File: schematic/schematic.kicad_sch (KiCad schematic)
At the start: 24 parts, among them SW1 SW_SPST, U1 ESP32-S3-DevKitC

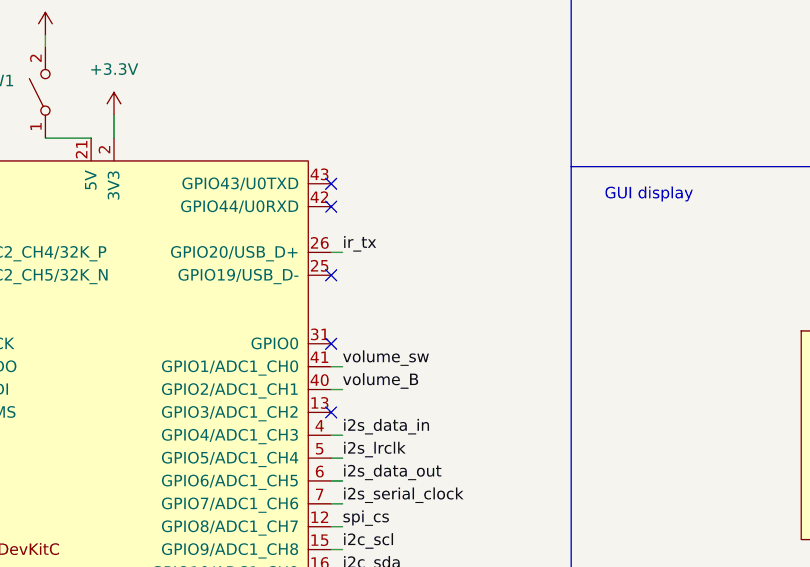
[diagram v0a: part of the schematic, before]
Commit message: Add pullup resistor to gpio 0.  This ensures that strapping pin gpio 0 is high when booting from external 5V supply.  In breadboard testing this did not affect booting from USB jack.
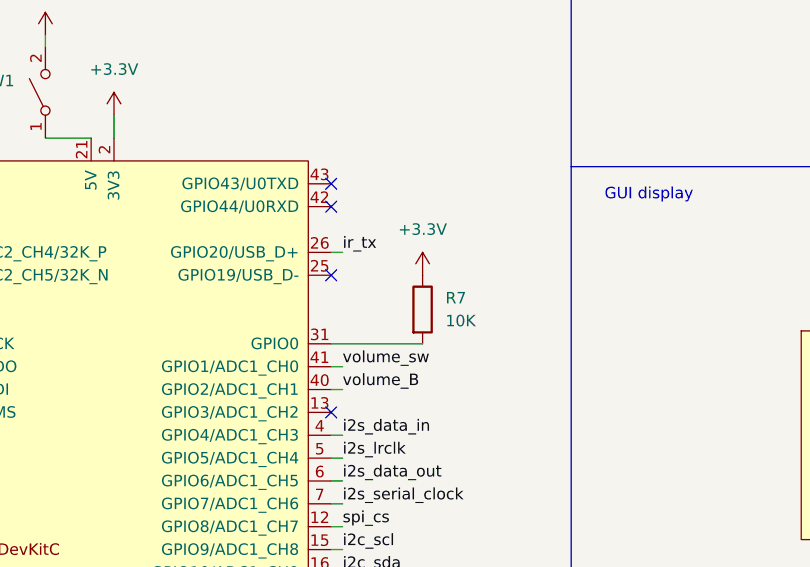
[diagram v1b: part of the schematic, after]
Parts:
- added R7: 10K, symbol Device:R
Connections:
- net +3.3V: now also R7.1
- net at U1.31 (GPIO0): now also R7.2
- no-connect marks 24 -> 23
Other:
- title: Internet Radio V2 -> Internet Radio V3
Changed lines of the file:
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@@
 	(paper "USLetter")
 	(title_block
-		(title "Internet Radio V2")
-		(date "2025-12-01")
-		(rev "2.0")
+		(title "Internet Radio V3")
+		(date "2026-02-24")
+		(rev "3.0")
 		(company "AG Keck")
 	)
@@
 	)
 	(no_connect
-		(at 157.48 99.06)
-	)
-	(no_connect
 		(at 106.68 81.28)
 	)
@@
 	(wire
 		(pts
+			(xy 157.48 99.06) (xy 167.64 99.06)
+		)
+		(stroke
+			(width 0)
+			(type default)
+		)
+	)
+	(wire
+		(pts
 			(xy 229.87 57.15) (xy 234.95 57.15)
 		)
@@
 	)
 	(symbol
+		(lib_id "Device:R")
+		(at 167.64 95.25 0)
+		(unit 1)
+		(exclude_from_sim no)
+		(in_bom yes)
+		(on_board yes)
+		(dnp no)
+		(fields_autoplaced yes)
+		(property "Reference" "R7"
+			(at 170.18 93.9799 0)
+			(effects
+				(font
+					(size 1.27 1.27)
+				)
+				(justify left)
+			)
+		)
+		(property "Value" "10K"
+			(at 170.18 96.5199 0)
+			(effects
+				(font
+					(size 1.27 1.27)
+				)
+				(justify left)
+			)
+		)
+		(property "Footprint" ""
+			(at 165.862 95.25 90)
+			(effects
+				(font
+					(size 1.27 1.27)
+				)
+				(hide yes)
+			)
+		)
+		(property "Datasheet" "~"
+			(at 167.64 95.25 0)
+			(effects
+				(font
+					(size 1.27 1.27)
+				)
+				(hide yes)
+			)
+		)
+		(property "Description" "Resistor"
+			(at 167.64 95.25 0)
+			(effects
+				(font
+					(size 1.27 1.27)
+				)
+				(hide yes)
+			)
+		)
+		(pin "2"
+		)
+		(pin "1"
+		)
+		(instances
+			(project ""
+				(path "/ad99cfc7-1930-4a76-846f-3ad4dbd23fae"
+					(reference "R7")
+					(unit 1)
+				)
+			)
+		)
+	)
+	(symbol
 		(lib_id "power:GND")
 		(at 49.53 97.79 90)
@@
 					(unit 1)
 				)
+			)
+		)
+	)
+	(symbol
+		(lib_id "power:+3.3V")
+		(at 167.64 91.44 0)
+		(unit 1)
+		(exclude_from_sim no)
+		(in_bom yes)
+		(on_board yes)
+		(dnp no)
+		(fields_autoplaced yes)
+		(property "Reference" "#PWR029"
+			(at 167.64 95.25 0)
+			(effects
+				(font
+					(size 1.27 1.27)
+				)
+				(hide yes)
+			)
+		)
+		(property "Value" "+3.3V"
+			(at 167.64 86.36 0)
+			(effects
+				(font
+					(size 1.27 1.27)
+				)
+			)
+		)
+		(property "Footprint" ""
+			(at 167.64 91.44 0)
+			(effects
+				(font
+					(size 1.27 1.27)
+				)
+				(hide yes)
+			)
+		)
+		(property "Datasheet" ""
+			(at 167.64 91.44 0)
+			(effects
+				(font
+					(size 1.27 1.27)
+				)
+				(hide yes)
+			)
+		)
+		(property "Description" "Power symbol creates a global label with name \"+3.3V\""
+			(at 167.64 91.44 0)
+			(effects
+				(font
+					(size 1.27 1.27)
+				)
+				(hide yes)
+			)
+		)
+		(pin "1"
+		)
+		(instances
+			(project ""
+				(path "/ad99cfc7-1930-4a76-846f-3ad4dbd23fae"
+					(reference "#PWR029")
+					(unit 1)
+				)
